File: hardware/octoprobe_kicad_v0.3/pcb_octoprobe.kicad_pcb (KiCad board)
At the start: 2 copper layers, 100 x 160 mm, 652 parts, among them J1001 Conn_01x20, J1002 Conn_01x20, J102 USB-226-BRW, J1101 Conn_01x20, J1102 Conn_01x20, J1103 Conn_01x20, J201 BOOT Button, J801 USB_C_Receptacle_USB2.0, Q201 NMOS, Q202 NMOS, SW201 RESET, U1201 MT9700, U201 RP2040, U202 AMS1117-3.3, U203 W25Q128JVS, U301 GAQY221S, U401 GAQY221S, U501 GAQY221S, U601 GAQY221S, U701 GAQY221S, U801 AMS1117-3.3, U802 USB2514B_Bi, U901 MT9700, Y201 Crystal_GND24_Small, Y801 24MHz

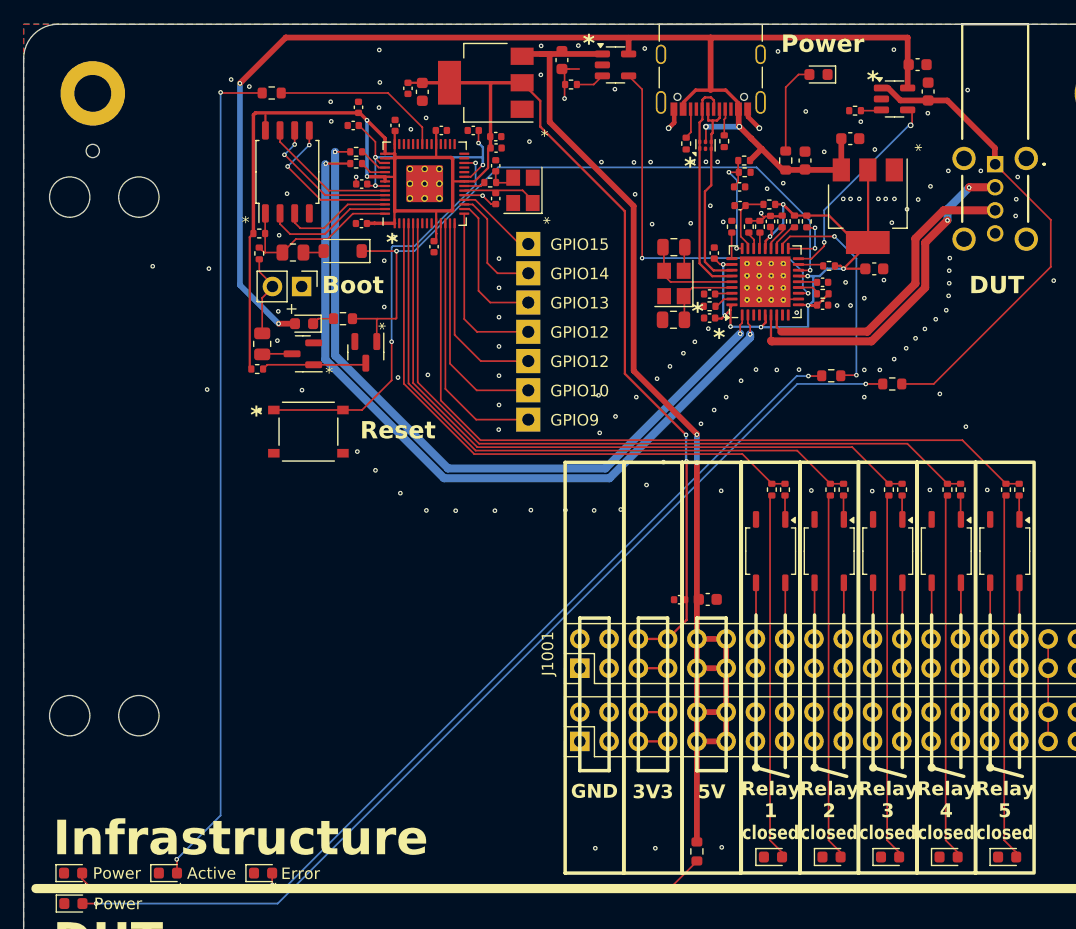
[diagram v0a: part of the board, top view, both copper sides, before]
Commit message: PCB: Move RP2
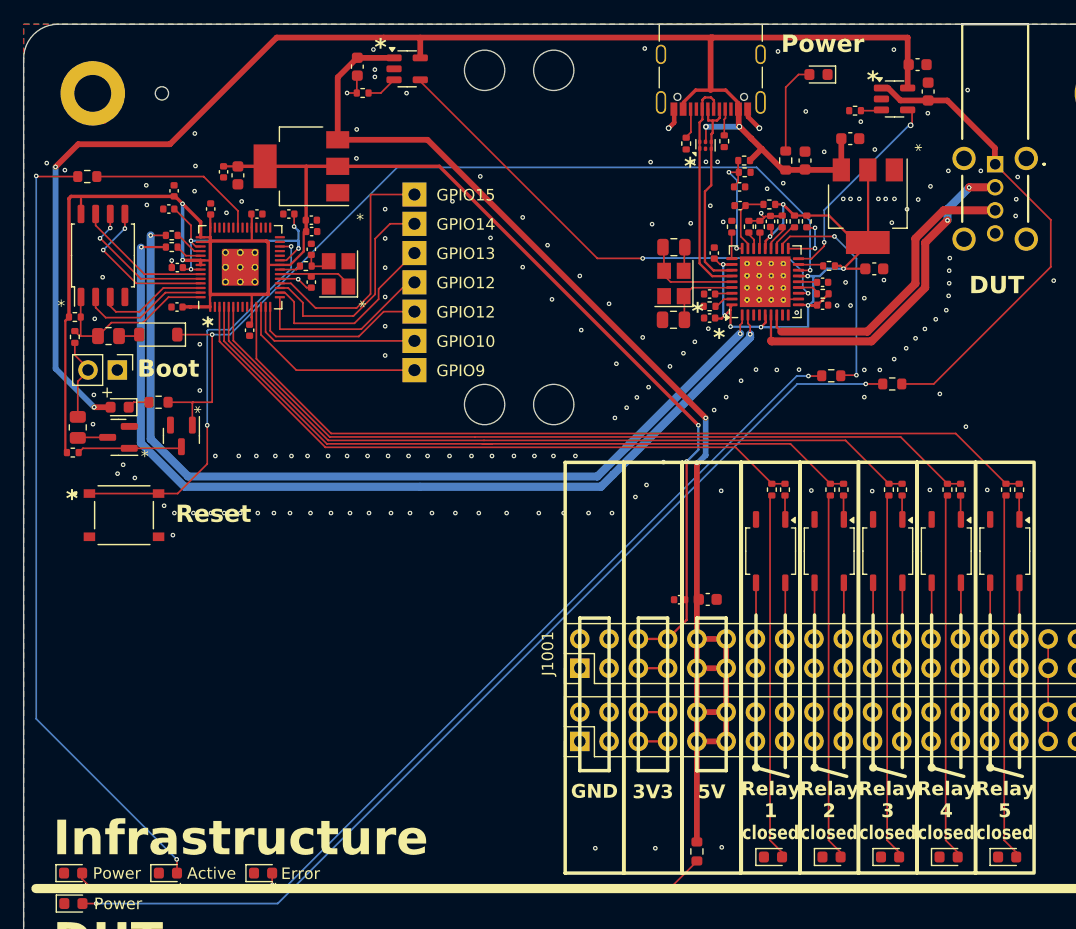
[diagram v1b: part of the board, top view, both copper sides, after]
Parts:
- moved H1103 45.0 mm to (114.0, 65.5)
- moved H1104 45.0 mm to (120.0, 65.5)
- moved H1101 37.6 mm to (114.0, 36.5)
- moved H1102 37.6 mm to (120.0, 36.5)
- moved R901 18.1 mm to (103.4, 38.5)
- moved U901 18.1 mm to (107.3, 36.4)
- moved C203 17.8 mm to (103.0, 36.2)
- moved C204 17.6 mm to (92.6, 45.6)
- moved C205 17.6 mm to (87.3, 53.6)
- moved C210 17.6 mm to (99.0, 50.5)
- moved C216 17.6 mm to (94.2, 49.0)
- moved D101 17.6 mm to (82.3, 65.7)
- moved D202 17.6 mm to (85.7, 59.4)
- moved R208 17.6 mm to (78.4, 57.9)
- moved R209 17.6 mm to (78.4, 59.6)
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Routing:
- net HUB+5V: track 120.7 -> 140.3 mm
- net RP2_BOOT: track 60.8 -> 79.8 mm
- net Net-(U201-GPIO15): track 6.38 -> 21.7 mm
- net RP2-USB-DM: track 64.7 -> 79.0 mm
- net RP2-USB-DP: track 67.3 -> 80.9 mm
- net /USB1_PWR: track 33.9 -> 43.5 mm
- net Net-(U201-GPIO14): track 10.3 -> 19.5 mm
- net +5V: track 100.2 -> 109.2 mm
- net RELAIS_2: track 55.2 -> 62.7 mm
- net RELAIS_5: track 68.6 -> 75.2 mm
- net RELAIS_4: track 64.6 -> 71.2 mm
- net RELAIS_3: track 59.9 -> 66.5 mm
- net RELAIS_1: track 50.6 -> 57.2 mm
- net Net-(U201-GPIO9): track 22.7 -> 17.0 mm
- net +3V3: track 179.6 -> 184.9 mm
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
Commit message: PCB: Octobus
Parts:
- added D1001: LED WHITE, 00_project_library:LED_0603_1608Metric, F.Cu at (164.2, 83.3)
- added D1401: LED WHITE, 00_project_library:LED_0603_1608Metric, F.Cu at (169.3, 83.3)
- added R1001: 2k2, Resistor_SMD:R_0805_2012Metric, F.Cu at (163.0, 72.6)
- added R1002: 390, Resistor_SMD:R_0805_2012Metric, F.Cu at (165.3, 72.6)
- added R1401: 2k2, Resistor_SMD:R_0805_2012Metric, F.Cu at (168.1, 72.6)
- added R1402: 390, Resistor_SMD:R_0805_2012Metric, F.Cu at (170.4, 72.6)
- added U1001: GAQY221S, 00_project_library:SOP-4_4.4x4.3mm_P2.54mm, F.Cu at (164.2, 78.2)
- added U1401: GAQY221S, 00_project_library:SOP-4_4.4x4.3mm_P2.54mm, F.Cu at (169.3, 78.2)
- added UR1001: 6, 00_project_library:opctoprobe_relay, F.Cu at (161.9, 106.2)
- added UR1401: 7, 00_project_library:opctoprobe_relay, F.Cu at (167.0, 106.2)
- BP203: value GPIO12 -> GPIO11
- J1101, J1102, J1103: footprint 00_project_library:PinSocket_2x20_P2.54mm_Vertical-mirrored-stackable -> 00_project_library:PinSocket_2x20_P2.54mm_Vertical-stackable_squarepad
- R301, R401, R501, R601, R701: footprint Resistor_SMD:R_0402_1005Metric -> Resistor_SMD:R_0805_2012Metric
- R302, R402, R502, R602, R702: value 3k9 -> 390; footprint Resistor_SMD:R_0402_1005Metric -> Resistor_SMD:R_0805_2012Metric
- U301, U401, U501, U601, U701: footprint Package_SO:SOP-4_3.8x4.1mm_P2.54mm -> 00_project_library:SOP-4_4.4x4.3mm_P2.54mm
- moved D301 21.5 mm to (138.8, 83.3)
- moved D401 21.5 mm to (143.9, 83.3)
- moved D501 21.5 mm to (149.0, 83.3)
- moved D601 21.5 mm to (154.0, 83.3)
- moved D701 21.5 mm to (159.1, 83.3)
- moved J1001 8.64 mm to (122.5, 94.5)
- moved J1002 8.64 mm to (122.5, 100.8)
- moved C212 5.59 mm to (129.6, 87.9)
- moved C902 5.46 mm to (133.4, 87.9)
- moved R104 3.05 mm to (133.9, 106.9), turned to 0 degrees
- moved R301 1.35 mm to (137.6, 72.6)
- moved R501 1.35 mm to (147.8, 72.6)
- moved R401 1.35 mm to (142.7, 72.6)
- moved R601 1.35 mm to (152.8, 72.6)
- moved R701 1.35 mm to (157.9, 72.6)
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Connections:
- net Net-(J1001-Pin_33) renamed /Relay Breakout/RELAY_OUT_6A
- net Net-(J1001-Pin_35) renamed /Relay Breakout/RELAY_OUT_6B
- net Net-(J1001-Pin_37) renamed /Relay Breakout/RELAY_OUT_7A
- net Net-(J1001-Pin_39) renamed /Relay Breakout/RELAY_OUT_7B
- J1101 pad 12: Net-(J1101-Pin_11) -> Net-(J1101-Pin_12)
- J1101 pad 14: Net-(J1101-Pin_13) -> Net-(J1101-Pin_14)
- J1101 pad 16: Net-(J1101-Pin_15) -> Net-(J1101-Pin_16)
- J1101 pad 18: Net-(J1101-Pin_17) -> Net-(J1101-Pin_18)
- J1101 pad 20: Net-(J1101-Pin_19) -> Net-(J1101-Pin_20)
- J1101 pad 22: Net-(J1101-Pin_21) -> Net-(J1101-Pin_22)
- J1101 pad 24: Net-(J1101-Pin_23) -> Net-(J1101-Pin_24)
- J1101 pad 26: Net-(J1101-Pin_25) -> Net-(J1101-Pin_26)
- J1101 pad 28: Net-(J1101-Pin_27) -> Net-(J1101-Pin_28)
- J1101 pad 30: Net-(J1101-Pin_29) -> Net-(J1101-Pin_30)
- J1101 pad 32: Net-(J1101-Pin_31) -> Net-(J1101-Pin_32)
- J1101 pad 34: Net-(J1101-Pin_33) -> Net-(J1101-Pin_34)
- J1101 pad 36: Net-(J1101-Pin_35) -> Net-(J1101-Pin_36)
- J1101 pad 6: Net-(J1101-Pin_5) -> Net-(J1101-Pin_6)
- J1101 pad 8: Net-(J1101-Pin_7) -> Net-(J1101-Pin_8)
- J1101 pad 9: Net-(J1101-Pin_10) -> Net-(J1101-Pin_9)
- J1102 pad 12: Net-(J1101-Pin_11) -> Net-(J1101-Pin_12)
- J1102 pad 14: Net-(J1101-Pin_13) -> Net-(J1101-Pin_14)
- J1102 pad 16: Net-(J1101-Pin_15) -> Net-(J1101-Pin_16)
- J1102 pad 18: Net-(J1101-Pin_17) -> Net-(J1101-Pin_18)
- J1102 pad 20: Net-(J1101-Pin_19) -> Net-(J1101-Pin_20)
- J1102 pad 22: Net-(J1101-Pin_21) -> Net-(J1101-Pin_22)
- J1102 pad 24: Net-(J1101-Pin_23) -> Net-(J1101-Pin_24)
- J1102 pad 26: Net-(J1101-Pin_25) -> Net-(J1101-Pin_26)
- J1102 pad 28: Net-(J1101-Pin_27) -> Net-(J1101-Pin_28)
- J1102 pad 30: Net-(J1101-Pin_29) -> Net-(J1101-Pin_30)
- J1102 pad 32: Net-(J1101-Pin_31) -> Net-(J1101-Pin_32)
- J1102 pad 34: Net-(J1101-Pin_33) -> Net-(J1101-Pin_34)
- J1102 pad 36: Net-(J1101-Pin_35) -> Net-(J1101-Pin_36)
- J1102 pad 6: Net-(J1101-Pin_5) -> Net-(J1101-Pin_6)
- J1102 pad 8: Net-(J1101-Pin_7) -> Net-(J1101-Pin_8)
- J1102 pad 9: Net-(J1101-Pin_10) -> Net-(J1101-Pin_9)
- J1103 pad 12: Net-(J1101-Pin_11) -> Net-(J1101-Pin_12)
- J1103 pad 14: Net-(J1101-Pin_13) -> Net-(J1101-Pin_14)
- J1103 pad 16: Net-(J1101-Pin_15) -> Net-(J1101-Pin_16)
- J1103 pad 18: Net-(J1101-Pin_17) -> Net-(J1101-Pin_18)
- J1103 pad 20: Net-(J1101-Pin_19) -> Net-(J1101-Pin_20)
- J1103 pad 22: Net-(J1101-Pin_21) -> Net-(J1101-Pin_22)
- J1103 pad 24: Net-(J1101-Pin_23) -> Net-(J1101-Pin_24)
- J1103 pad 26: Net-(J1101-Pin_25) -> Net-(J1101-Pin_26)
- J1103 pad 28: Net-(J1101-Pin_27) -> Net-(J1101-Pin_28)
- J1103 pad 30: Net-(J1101-Pin_29) -> Net-(J1101-Pin_30)
- J1103 pad 32: Net-(J1101-Pin_31) -> Net-(J1101-Pin_32)
- J1103 pad 34: Net-(J1101-Pin_33) -> Net-(J1101-Pin_34)
- J1103 pad 36: Net-(J1101-Pin_35) -> Net-(J1101-Pin_36)
- J1103 pad 6: Net-(J1101-Pin_5) -> Net-(J1101-Pin_6)
- J1103 pad 8: Net-(J1101-Pin_7) -> Net-(J1101-Pin_8)
- J1103 pad 9: Net-(J1101-Pin_10) -> Net-(J1101-Pin_9)
- U201 pad 11: RELAIS_5 -> unconnected-(U201-GPIO8-Pad11)
- U201 pad 7: unconnected-(U201-GPIO5-Pad7) -> RELAIS_5
- U201 pad 8: unconnected-(U201-GPIO6-Pad8) -> RELAIS_6
- U201 pad 9: unconnected-(U201-GPIO7-Pad9) -> RELAIS_7
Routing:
- net RELAIS_7: track 0.00 -> 84.7 mm
- net RELAIS_6: track 0.00 -> 80.1 mm
- net GND: track 53.3 -> 18.7 mm
- net Net-(D401-A): track 31.6 -> 10.6 mm
- net Net-(D601-A): track 31.6 -> 10.6 mm
- net Net-(D701-A): track 31.6 -> 10.6 mm
- net Net-(D501-A): track 31.6 -> 10.6 mm
- net Net-(D301-A): track 31.6 -> 10.6 mm
- net Net-(J1101-Pin_9): track 0.00 -> 17.5 mm
- net Net-(J1101-Pin_8): track 0.00 -> 16.5 mm
- net Net-(J1101-Pin_34): track 0.00 -> 16.5 mm
- net Net-(J1101-Pin_32): track 0.00 -> 16.5 mm
- net Net-(J1101-Pin_26): track 0.00 -> 16.5 mm
- net Net-(J1101-Pin_24): track 0.00 -> 16.5 mm
- net Net-(J1101-Pin_20): track 0.00 -> 16.5 mm
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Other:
- board text added: "10"
- board text added: "20"
- board text added: "30"
- board text added: "40"

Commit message: PCB: Oscillator
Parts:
- removed C201, C202: 30p, Capacitor_SMD:C_0402_1005Metric
- removed R201: 1k, Resistor_SMD:R_0402_1005Metric
- removed Y201: Crystal_GND24_Small, 00_project_library:Crystal_SMD_3225-4Pin_3.2x2.5mm
- added X201: Oscillator-12MHz, Oscillator:Oscillator_SMD_ECS_2520MV-xxx-xx-4Pin_2.5x2.0mm, F.Cu at (100.5, 53.5)
- R104, R202: footprint Resistor_SMD:R_0603_1608Metric -> Resistor_SMD:R_0805_2012Metric
- R1201, R901: footprint Resistor_SMD:R_0402_1005Metric -> Resistor_SMD:R_0805_2012Metric
- UR1001, UR1401, UR301, UR401, UR501, UR601, UR701: footprint 00_project_library:opctoprobe_relay -> 00_project_library:octoprobe_relay
- moved R901 1.02 mm to (104.1, 39.2)
- moved R1201 0.64 mm to (145.5, 40.0)
- moved C806 0.50 mm to (136.6, 46.4)
- moved R202 0.32 mm to (79.8, 45.7)
- moved C805 0.10 mm to (136.2, 48.1)
- moved R805 0.07 mm to (136.6, 44.3)
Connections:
- U201 pad 21: /RP2 CPU/XOUT -> unconnected-(U201-XOUT-Pad21)
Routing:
- net +3V3: track 193.8 -> 201.7 mm
- net Net-(U201-GPIO12): track 16.1 -> 13.0 mm
- net Net-(U201-GPIO13): track 16.9 -> 13.8 mm
- net GND: track 18.7 -> 15.7 mm, vias 174 -> 172
- net Net-(U201-GPIO14): track 19.5 -> 16.5 mm
- net /RP2 CPU/XIN: track 6.28 -> 3.39 mm
- net Net-(U201-GPIO15): track 21.7 -> 19.1 mm
- net Net-(U201-GPIO11): track 15.7 -> 13.4 mm
- net Net-(C202-Pad1): track 2.07 -> 0.00 mm
- net /RP2 CPU/XOUT: track 1.87 -> 0.00 mm
- net Net-(U901-SET): track 2.69 -> 2.00 mm
- net Net-(U201-GPIO10): track 15.4 -> 14.8 mm
